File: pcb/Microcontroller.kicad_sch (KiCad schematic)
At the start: 36 parts, among them J1 ISP, Q2 BC817, Q3 BC817, Q4 BC817, SW2 RESET, SW3 START, SW4 STOP, U4 ATmega328P-A, Y1 15MHz

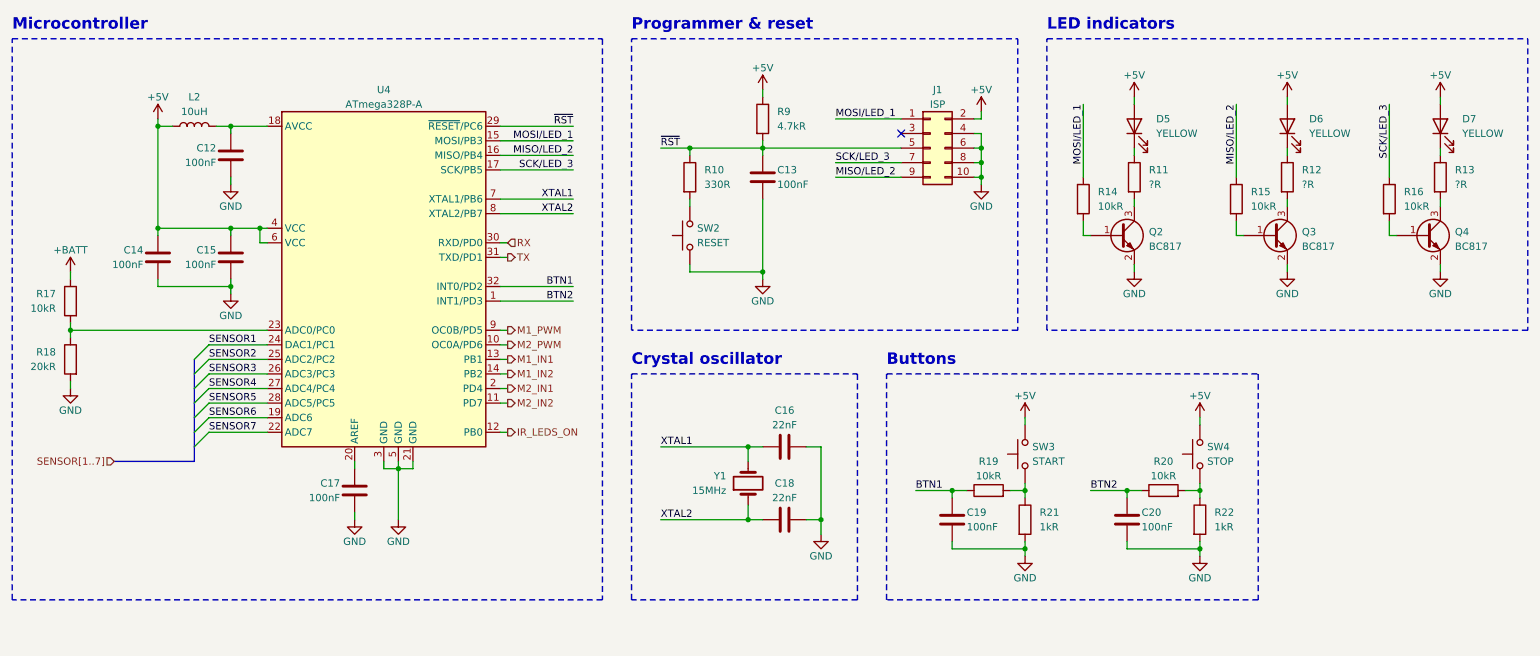
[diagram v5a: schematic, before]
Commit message: [pcb] Rework schematic for ATxmega16A4U
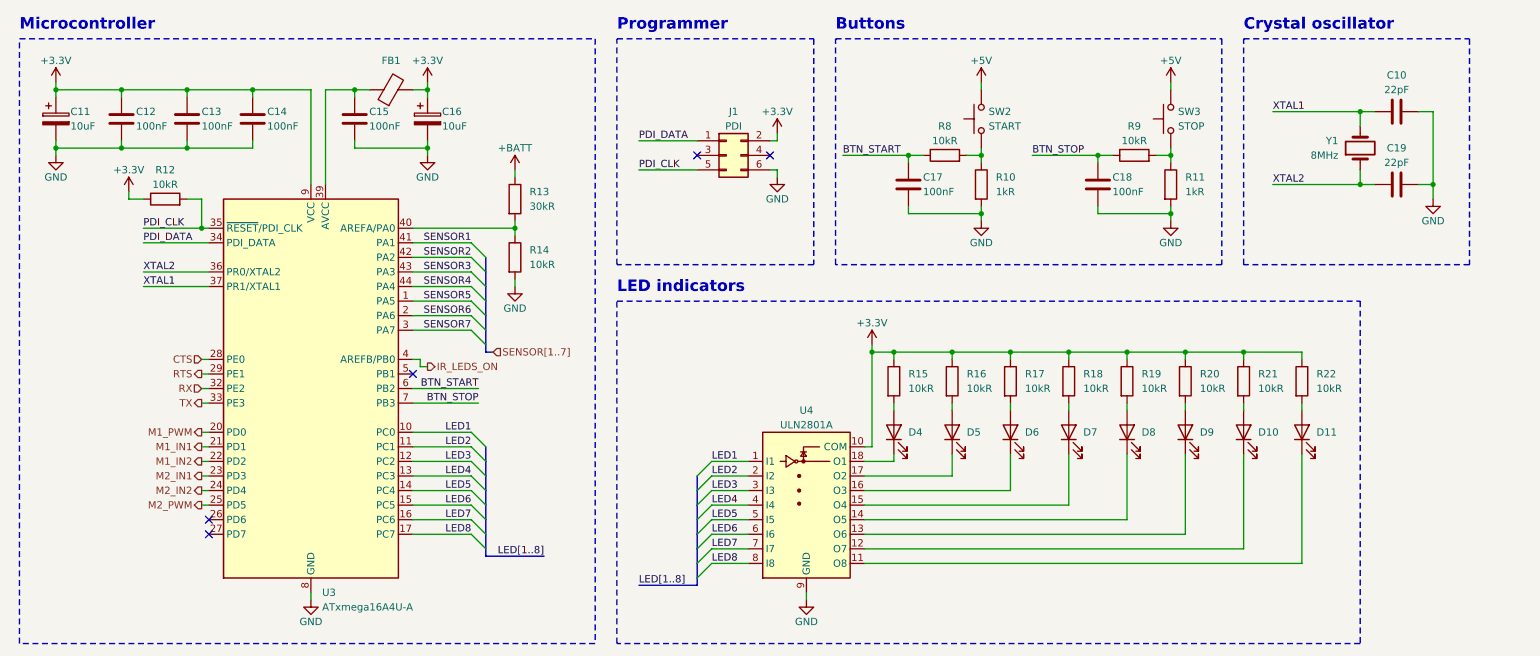
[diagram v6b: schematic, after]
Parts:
- removed C17: 100nF, Capacitor_SMD:C_0805_2012Metric, symbol Device:C
- removed J1: ISP, Connector_IDC:IDC-Header_2x05_P2.54mm_Vertical, symbol Connector_Generic:Conn_02x05_Odd_Even
- removed L2: 10uH, Inductor_SMD:L_0805_2012Metric, symbol Device:L
- removed Q2, Q3, Q4: BC817, Package_TO_SOT_SMD:SOT-23, symbol Transistor_BJT:BC817
- removed R10: 330R, Resistor_SMD:R_0805_2012Metric, symbol Device:R
- removed R11, R13: ?R, Resistor_SMD:R_0805_2012Metric, symbol Device:R
- removed R14: 10kR, Resistor_SMD:R_0805_2012Metric, symbol Device:R
- removed R9: 4.7kR, Resistor_SMD:R_0805_2012Metric, symbol Device:R
- removed SW2: RESET, Button_Switch_THT:SW_PUSH_6mm_H5mm, symbol Switch:SW_Push
- removed U4: ATmega328P-A, Package_QFP:TQFP-32_7x7mm_P0.8mm, symbol MCU_Microchip_ATmega:ATmega328P-A
- added C11, C16: 10uF, symbol Device:C_Polarized
- added D10, D11, D4, D8, D9: YELLOW, LED_SMD:LED_0805_2012Metric, symbol Device:LED
- added FB1: FerriteBead, symbol Device:FerriteBead
- added J1: PDI, Connector_IDC:IDC-Header_2x03_P2.54mm_Vertical, symbol Connector_Generic:Conn_02x03_Odd_Even
- added R17, R18, R19, R20, R21, R22: 10kR, Resistor_SMD:R_0805_2012Metric, symbol Device:R
- added U3: ATxmega16A4U-A, Package_QFP:TQFP-44_10x10mm_P0.8mm, symbol MCU_Microchip_ATmega:ATxmega16A4U-A
- added U4: ULN2801A, symbol Transistor_Array:ULN2801A
- C10: renamed from C16; value 22nF -> 22pF
- C19: renamed from C18; value 22nF -> 22pF
- R12: value ?R -> 10kR
- R13: renamed from R18; value 20kR -> 30kR
- Y1: value 15MHz -> 8MHz
- renumbered C19 to C17, C20 to C18, R21 to R10, R22 to R11, R17 to R14, R19 to R8, R20 to R9, SW3 to SW2, SW4 to SW3
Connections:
- net MISO/LED_2 is gone; now on net +3.3V: R15.1
- net SCK/LED_3 is gone; now on net +3.3V: R16.1
- net ~{RST} is gone; now on net +3.3V: C13.1
- net +5V: no longer C14.1, C15.1, D5.2 (A), D6.2 (A), D7.2 (A)
- net +BATT: now also R13.1; no longer R14.1
- net GND: now also R14.2, C11.2, C16.2, J1.6 (Pin_6), U3.18 (GND), U3.30 (GND), U3.38 (GND), U3.8 (GND), U4.9 (GND); no longer R13.2
- net IR_LEDS_ON: now also U3.4 (AREFB/PB0)
- net M1_IN1: now also U3.21 (PD1)
- net M1_IN2: now also U3.22 (PD2)
- net M1_PWM: now also U3.20 (PD0)
- net M2_IN1: now also U3.23 (PD3)
- net M2_IN2: now also U3.24 (PD4)
- net M2_PWM: now also U3.25 (PD5)
- net RX: now also U3.32 (PE2)
- net SENSOR1: now also U3.41 (PA1)
- net SENSOR2: now also U3.42 (PA2)
- net SENSOR3: now also U3.43 (PA3)
- net SENSOR4: now also U3.44 (PA4)
- net SENSOR5: now also U3.1 (PA5)
- net SENSOR6: now also U3.2 (PA6)
- net SENSOR7: now also U3.3 (PA7)
- net TX: now also U3.33 (PE3)
- net XTAL1: now also U3.37 (PR1/XTAL1)
- net XTAL2: now also U3.36 (PR0/XTAL2)
- net at D5.1 (K): now also U4.17 (O2)
- net at D7.1 (K): now also U4.15 (O4)
- net +3.3V: now reaches C12.1
- net +3.3V: now also C14.1, R12.1, C11.1, C16.1, FB1.2, J1.2 (Pin_2), R17.1, R18.1, R19.1, R20.1, R21.1, R22.1, U3.19 (VCC), U3.31 (VCC), U3.9 (VCC), U4.10 (COM)
- net at R15.2: now also D4.2 (A)
- net PDI_CLK: now reaches R12.2
- net PDI_CLK: now also J1.5 (Pin_5), U3.35 (~{RESET}/PDI_CLK)
- net at R16.2: now also D5.2 (A)
- net at D6.1 (K): now also U4.16 (O3); no longer R12.1
- net BTN1 renamed BTN_START
- net BTN_START: now also U3.6 (PB2)
- net BTN2 renamed BTN_STOP
- net BTN_STOP: now also U3.7 (PB3)
- new net: D6.2 (A), R17.2
- new net: D7.2 (A), R18.2
- new net: D9.1 (K), U4.13 (O6)
- new net: D9.2 (A), R20.2
- new net: C15.1, FB1.1, U3.39 (AVCC)
- new net: D11.1 (K), U4.11 (O8)
- new net: D10.1 (K), U4.12 (O7)
- new net: D8.1 (K), U4.14 (O5)
- new net: D4.1 (K), U4.18 (O1)
- new net: D11.2 (A), R22.2
- new net: D8.2 (A), R19.2
- new net: R13.2, R14.1, U3.40 (AREFA/PA0)
- new net: D10.2 (A), R21.2
- new net CTS: U3.28 (PE0)
- new net LED1: U3.10 (PC0), U4.1 (I1)
- new net LED2: U3.11 (PC1), U4.2 (I2)
- new net LED3: U3.12 (PC2), U4.3 (I3)
- new net LED4: U3.13 (PC3), U4.4 (I4)
- new net LED5: U3.14 (PC4), U4.5 (I5)
- new net LED6: U3.15 (PC5), U4.6 (I6)
- new net LED7: U3.16 (PC6), U4.7 (I7)
- new net LED8: U3.17 (PC7), U4.8 (I8)
- new net PDI_DATA: J1.1 (Pin_1), U3.34 (PDI_DATA)
- new net RTS: U3.29 (PE1)
- no-connect marks 1 -> 5
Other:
- note added: "Programmer"
- note removed: "Programmer & reset"
- moved on the sheet: C10, C17, C18, C19, R10, R11, R13, R14, R8, R9, SW2, SW3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

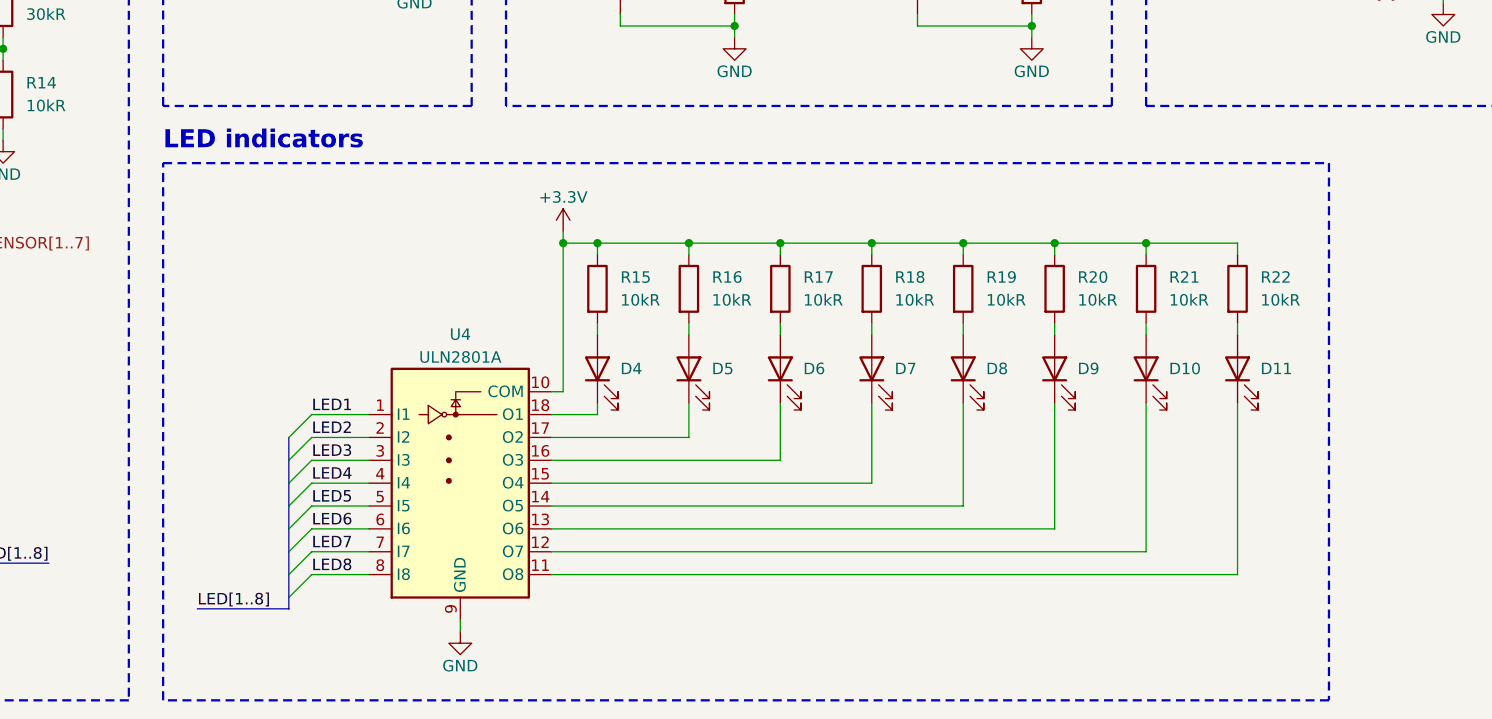
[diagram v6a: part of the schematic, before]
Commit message: Power switch footprint and initial pcb
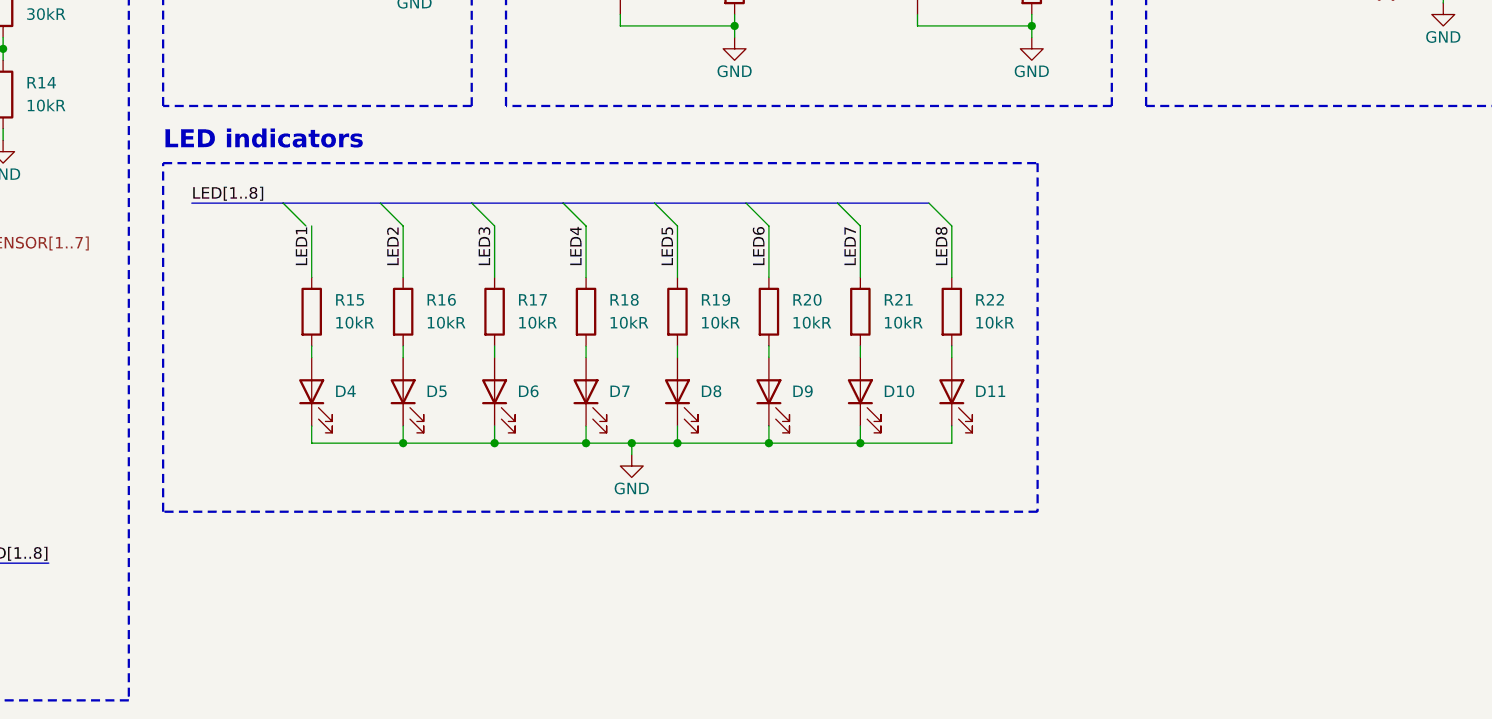
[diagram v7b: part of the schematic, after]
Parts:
- removed U4: ULN2801A, symbol Transistor_Array:ULN2801A
- C11, C16: footprint (none) -> Capacitor_Tantalum_SMD:CP_EIA-3216-18_Kemet-A
- FB1: footprint (none) -> Inductor_SMD:L_0805_2012Metric
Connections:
- net +3.3V: no longer R15.1, R16.1, R17.1, R18.1, R19.1, R20.1, R21.1, R22.1
- net GND: now also D10.1 (K), D11.1 (K), D4.1 (K), D5.1 (K), D6.1 (K), D7.1 (K), D8.1 (K), D9.1 (K)
- net LED1: now also R15.1
- net LED2: now also R16.1
- net LED3: now also R17.1
- net LED4: now also R18.1
- net LED5: now also R19.1
- net LED6: now also R20.1
- net LED7: now also R21.1
- net LED8: now also R22.1
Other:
- moved on the sheet: D10, D11, D4, D5, D6, D7, D8, D9, R15, R16, R17, R18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

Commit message: [pcb] Initial layout
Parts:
- R15, R16, R17, R18, R19, R20, R21, R22: value 10kR -> ???R
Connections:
- net GND: now also R15.2, R16.2, R17.2, R18.2, R19.2, R20.2, R21.2, R22.2; no longer D10.1 (K), D11.1 (K), D4.1 (K), D5.1 (K), D6.1 (K), D7.1 (K), D8.1 (K), D9.1 (K)
- net LED1: now also D4.2 (A); no longer R15.1
- net LED2: now also D5.2 (A); no longer R16.1
- net LED3: now also D6.2 (A); no longer R17.1
- net LED4: now also D7.2 (A); no longer R18.1
- net LED5: now also D8.2 (A); no longer R19.1
- net LED6: now also D9.2 (A); no longer R20.1
- net LED7: now also D10.2 (A); no longer R21.1
- net LED8: now also D11.2 (A); no longer R22.1
- net SENSOR1: now also U3.2 (PA6); no longer U3.41 (PA1)
- net SENSOR2: now also U3.1 (PA5); no longer U3.42 (PA2)
- net SENSOR3: now also U3.44 (PA4); no longer U3.43 (PA3)
- net SENSOR4: now also U3.43 (PA3); no longer U3.44 (PA4)
- net SENSOR5: now also U3.42 (PA2); no longer U3.1 (PA5)
- net SENSOR6: now also U3.41 (PA1); no longer U3.2 (PA6)
- net SENSOR7: now also U3.40 (AREFA/PA0); no longer U3.3 (PA7)
- net at R13.2, R14.1: now also U3.3 (PA7); no longer U3.40 (AREFA/PA0)
- new net: D4.1 (K), R15.1
- new net: D6.1 (K), R17.1
- new net: D7.1 (K), R18.1
- new net: D9.1 (K), R20.1
- new net: D11.1 (K), R22.1
- new net: D8.1 (K), R19.1
- new net: D10.1 (K), R21.1
- new net: D5.1 (K), R16.1
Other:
- moved on the sheet: D10, D11, D4, D5, D6, D7, D8, D9, R13, R14, R15, R16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
